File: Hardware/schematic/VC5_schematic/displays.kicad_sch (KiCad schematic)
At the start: 5 parts, among them U1 1.3in SH1106 OLED, U2 1.3in SH1106 OLED, U3 1.3in SH1106 OLED, U4 1.3in SH1106 OLED, U5 1.3in SH1106 OLED

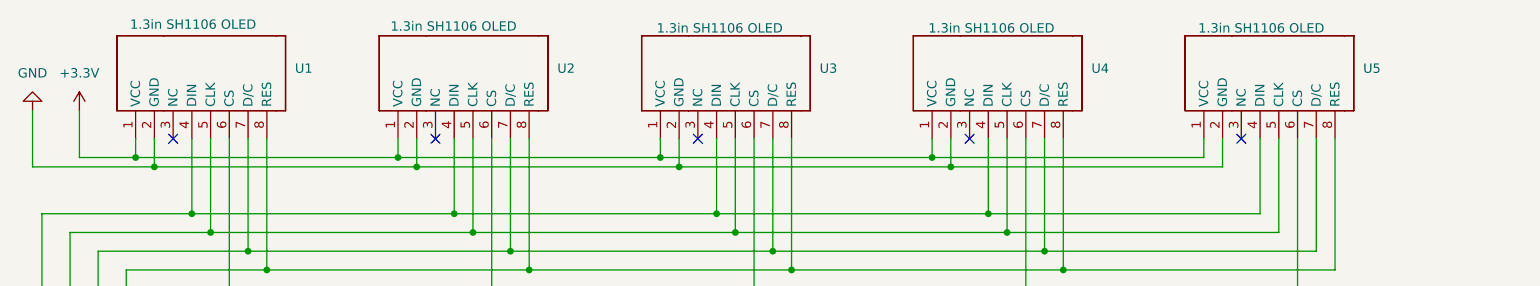
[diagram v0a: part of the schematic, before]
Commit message: fixed missing schematic symbols
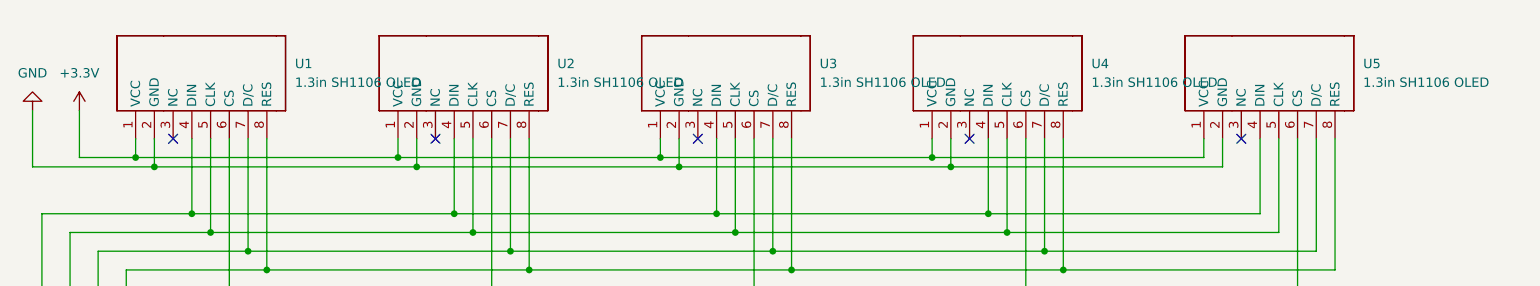
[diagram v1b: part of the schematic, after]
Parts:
- removed U1, U2, U3, U4, U5: 1.3in SH1106 OLED, symbol VC5_display:Display,_8_pin
- added U1, U2, U3, U4, U5: 1.3in SH1106 OLED, symbol VC5_library:Waveshare-Display-1_3in-SH1106-OLED
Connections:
- net +3.3V: now also U1.1 (VCC), U2.1 (VCC), U3.1 (VCC), U4.1 (VCC), U5.1 (VCC)
- net CLK: now also U1.5 (CLK), U2.5 (CLK), U3.5 (CLK), U4.5 (CLK), U5.5 (CLK)
- net CS0: now also U1.6 (CS)
- net CS1: now also U2.6 (CS)
- net CS2: now also U3.6 (CS)
- net CS3: now also U4.6 (CS)
- net CS4: now also U5.6 (CS)
- net DIN: now also U1.4 (DIN), U2.4 (DIN), U3.4 (DIN), U4.4 (DIN), U5.4 (DIN)
- net DISP_RESET: now also U1.8 (RES), U2.8 (RES), U3.8 (RES), U4.8 (RES), U5.8 (RES)
- net D/C: now also U1.7 (D/C), U2.7 (D/C), U3.7 (D/C), U4.7 (D/C), U5.7 (D/C)
- net GND: now also U1.2 (GND), U2.2 (GND), U3.2 (GND), U4.2 (GND), U5.2 (GND)

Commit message: fixed an error in the filters for the rotaries
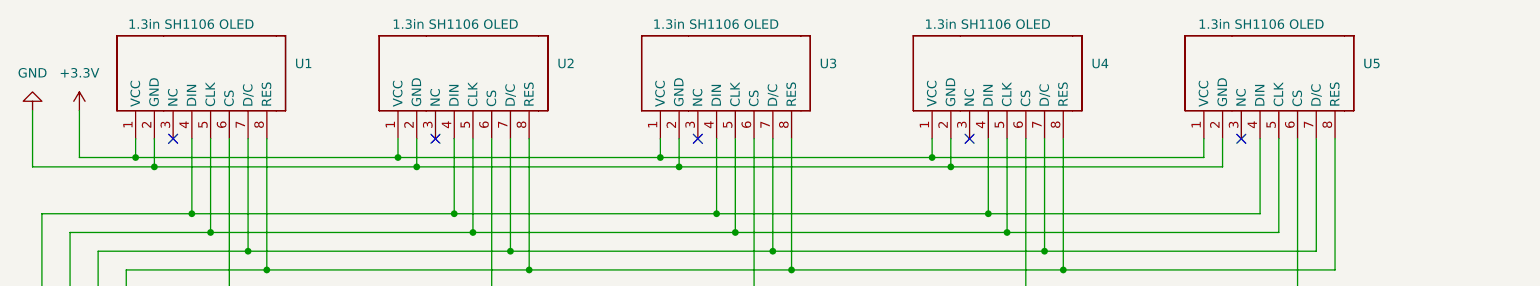
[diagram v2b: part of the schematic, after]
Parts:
- U1, U2, U3, U4, U5: footprint (none) -> Connector_PinHeader_2.54mm:PinHeader_1x08_P2.54mm_Vertical
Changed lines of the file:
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@@
 		(on_board yes)
 		(dnp no)
-		(fields_autoplaced yes)
 		(property "Reference" "U5"
 			(at 242.57 50.7999 0)
@@
 		)
 		(property "Value" "1.3in SH1106 OLED"
-			(at 242.57 53.3399 0)
-			(effects
-				(font
-					(size 1.27 1.27)
-				)
-				(justify left)
-			)
-		)
-		(property "Footprint" ""
+			(at 220.218 45.466 0)
+			(effects
+				(font
+					(size 1.27 1.27)
+				)
+				(justify left)
+			)
+		)
+		(property "Footprint" "Connector_PinHeader_2.54mm:PinHeader_1x08_P2.54mm_Vertical"
 			(at 242.57 49.53 0)
 			(effects
@@
 		(on_board yes)
 		(dnp no)
-		(fields_autoplaced yes)
 		(property "Reference" "U1"
 			(at 97.79 50.7999 0)
@@
 		)
 		(property "Value" "1.3in SH1106 OLED"
-			(at 97.79 53.3399 0)
-			(effects
-				(font
-					(size 1.27 1.27)
-				)
-				(justify left)
-			)
-		)
-		(property "Footprint" ""
+			(at 75.184 45.466 0)
+			(effects
+				(font
+					(size 1.27 1.27)
+				)
+				(justify left)
+			)
+		)
+		(property "Footprint" "Connector_PinHeader_2.54mm:PinHeader_1x08_P2.54mm_Vertical"
 			(at 97.79 49.53 0)
 			(effects
@@
 		(on_board yes)
 		(dnp no)
-		(fields_autoplaced yes)
 		(property "Reference" "U2"
 			(at 133.35 50.7999 0)
@@
 		)
 		(property "Value" "1.3in SH1106 OLED"
-			(at 133.35 53.3399 0)
-			(effects
-				(font
-					(size 1.27 1.27)
-				)
-				(justify left)
-			)
-		)
-		(property "Footprint" ""
+			(at 110.998 45.466 0)
+			(effects
+				(font
+					(size 1.27 1.27)
+				)
+				(justify left)
+			)
+		)
+		(property "Footprint" "Connector_PinHeader_2.54mm:PinHeader_1x08_P2.54mm_Vertical"
 			(at 133.35 49.53 0)
 			(effects
@@
 		(on_board yes)
 		(dnp no)
-		(fields_autoplaced yes)
 		(property "Reference" "U4"
 			(at 205.74 50.7999 0)
@@
 		)
 		(property "Value" "1.3in SH1106 OLED"
-			(at 205.74 53.3399 0)
-			(effects
-				(font
-					(size 1.27 1.27)
-				)
-				(justify left)
-			)
-		)
-		(property "Footprint" ""
+			(at 183.134 45.466 0)
+			(effects
+				(font
+					(size 1.27 1.27)
+				)
+				(justify left)
+			)
+		)
+		(property "Footprint" "Connector_PinHeader_2.54mm:PinHeader_1x08_P2.54mm_Vertical"
 			(at 205.74 49.53 0)
 			(effects
@@
 		(on_board yes)
 		(dnp no)
-		(fields_autoplaced yes)
 		(property "Reference" "U3"
 			(at 168.91 50.7999 0)
@@
 		)
 		(property "Value" "1.3in SH1106 OLED"
-			(at 168.91 53.3399 0)
-			(effects
-				(font
-					(size 1.27 1.27)
-				)
-				(justify left)
-			)
-		)
-		(property "Footprint" ""
+			(at 146.304 45.466 0)
+			(effects
+				(font
+					(size 1.27 1.27)
+				)
+				(justify left)
+			)
+		)
+		(property "Footprint" "Connector_PinHeader_2.54mm:PinHeader_1x08_P2.54mm_Vertical"
 			(at 168.91 49.53 0)
 			(effects

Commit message: updated footprints and corresponding 3D models
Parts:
- U1, U2, U3, U4, U5: footprint Connector_PinHeader_2.54mm:PinHeader_1x08_P2.54mm_Vertical -> VC5_footprint_library:PinHeader_1x08_P2.54mm_Vertical_Display
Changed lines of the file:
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@@
 			)
 		)
-		(property "Footprint" "Connector_PinHeader_2.54mm:PinHeader_1x08_P2.54mm_Vertical"
+		(property "Footprint" "VC5_footprint_library:PinHeader_1x08_P2.54mm_Vertical_Display"
 			(at 242.57 49.53 0)
 			(effects
@@
 			)
 		)
-		(property "Footprint" "Connector_PinHeader_2.54mm:PinHeader_1x08_P2.54mm_Vertical"
+		(property "Footprint" "VC5_footprint_library:PinHeader_1x08_P2.54mm_Vertical_Display"
 			(at 97.79 49.53 0)
 			(effects
@@
 			)
 		)
-		(property "Footprint" "Connector_PinHeader_2.54mm:PinHeader_1x08_P2.54mm_Vertical"
+		(property "Footprint" "VC5_footprint_library:PinHeader_1x08_P2.54mm_Vertical_Display"
 			(at 133.35 49.53 0)
 			(effects
@@
 			)
 		)
-		(property "Footprint" "Connector_PinHeader_2.54mm:PinHeader_1x08_P2.54mm_Vertical"
+		(property "Footprint" "VC5_footprint_library:PinHeader_1x08_P2.54mm_Vertical_Display"
 			(at 205.74 49.53 0)
 			(effects
@@
 			)
 		)
-		(property "Footprint" "Connector_PinHeader_2.54mm:PinHeader_1x08_P2.54mm_Vertical"
+		(property "Footprint" "VC5_footprint_library:PinHeader_1x08_P2.54mm_Vertical_Display"
 			(at 168.91 49.53 0)
 			(effects
